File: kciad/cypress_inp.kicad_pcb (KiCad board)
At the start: 2 copper layers, 146.3 x 61.2 mm, 57 parts, among them J1 Cypress CY7C68013A Left Bot, J10 Conn_01x03_Male, J11 Conn_01x03_Male, J2 Connector PDx, J3 Cypress CY7C68013A Right Bot, J4 Connector PBx, J5 Power, J6 USB_B, J7 Conn_01x04_Male, J8 Conn_01x03_Male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

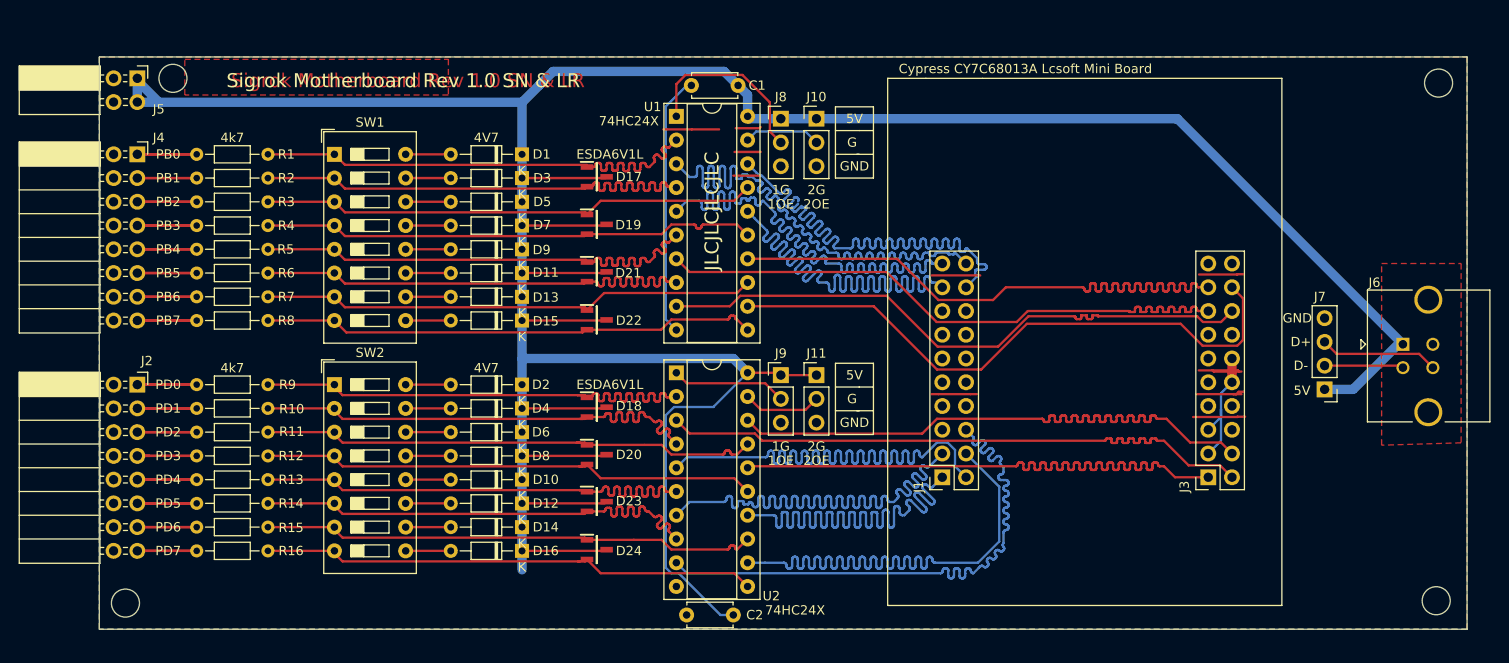
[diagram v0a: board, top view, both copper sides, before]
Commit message: * changed layout so signal paths are shorter
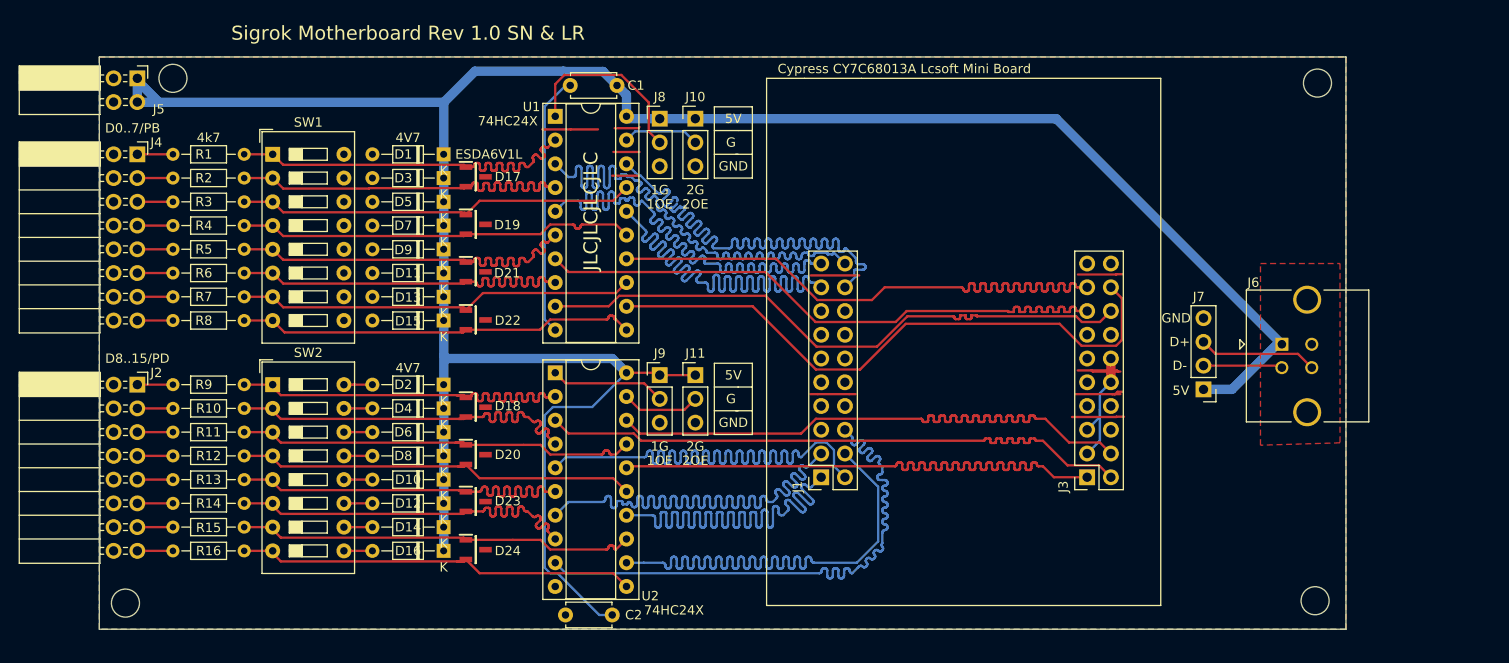
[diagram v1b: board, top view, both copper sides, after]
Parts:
- moved J1 13.0 mm to (136.4, 114.3)
- moved J3 13.0 mm to (164.8, 114.3)
- moved J7 13.0 mm to (177.3, 104.9)
- moved J8 13.0 mm to (119.1, 75.9)
- moved J9 13.0 mm to (119.1, 103.4)
- moved C1 13.0 mm to (114.6, 72.4)
- moved C2 13.0 mm to (114.0, 129.0)
- moved D17 13.0 mm to (99.4, 82.2)
- moved D18 13.0 mm to (99.4, 106.8)
- moved D19 13.0 mm to (99.4, 87.2)
- moved D20 13.0 mm to (99.4, 111.9)
- moved D21 13.0 mm to (99.4, 92.3)
- moved D22 13.0 mm to (99.4, 97.5)
- moved D23 13.0 mm to (99.4, 116.9)
- moved D24 13.0 mm to (99.4, 122.0)
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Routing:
- net +5V: track 360.7 -> 269.6 mm
- net B-PD0: track 15.7 -> 3.81 mm
- net /U1-1A0: track 53.1 -> 42.8 mm
- net /U1-2A0: track 53.9 -> 43.7 mm
- net /U2-2A2: track 53.2 -> 43.1 mm
- net /U2-2A1: track 53.2 -> 43.0 mm
- net /U1-1A2: track 53.0 -> 42.9 mm
- net /U1-1A1: track 53.3 -> 43.2 mm
- net /U1-1A3: track 53.3 -> 43.2 mm
- net /U1-2A2: track 53.0 -> 43.0 mm
- net /U1-2A1: track 53.6 -> 43.6 mm
- net /U2-1A0: track 53.6 -> 43.7 mm
- net /U1-2A3: track 53.3 -> 43.5 mm
- net B-PD3: track 13.5 -> 3.81 mm
- net B-PD1: track 13.5 -> 3.81 mm
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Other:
- board size 146.3 x 61.2 mm -> 133.4 x 61.2 mm
- board text added: "D0..7/PB"
- board text added: "D8..15/PD"
- board text removed: "PB0"
- board text removed: "PB1"
- board text removed: "PB2"
- board text removed: "PB3"
- board text removed: "PB4"
- board text removed: "PB5"
- board text removed: "PB6"
- board text removed: "PB7"
- board text removed: "PD0"
- board text removed: "PD1"
- board text removed: "PD2"
- board text removed: "PD3"
- board text removed: "PD4"
- board text removed: "PD5"
- board text removed: "PD6"
- board text removed: "PD7"

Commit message: * changed whole schematic and pcb layout
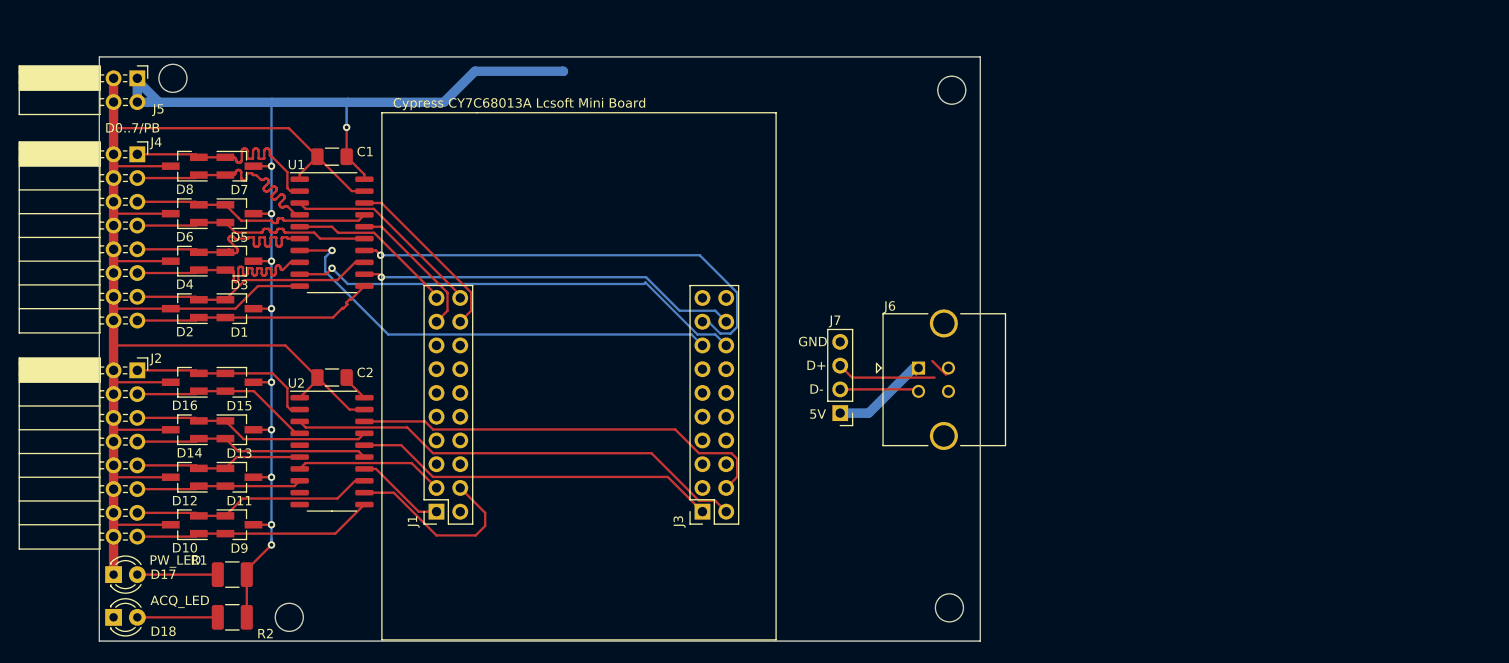
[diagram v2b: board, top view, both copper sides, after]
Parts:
- removed D19, D20, D21, D22, D23, D24: ESDA6V1L, SamacSys_Parts:SOT105P242X150-3N
- removed J10, J11, J8, J9: Conn_01x03_Male, Connector_PinHeader_2.54mm:PinHeader_1x03_P2.54mm_Vertical
- removed R10, R11, R12, R13, R14, R15, R16, R3, R4, R5, R6, R7, R8, R9: 4k7, Resistor_THT:R_Axial_DIN0204_L3.6mm_D1.6mm_P7.62mm_Horizontal
- removed SW1, SW2: SW_DIP_x08, Button_Switch_THT:SW_DIP_SPSTx08_Slide_9.78x22.5mm_W7.62mm_P2.54mm
- C1, C2: value C -> 100nF; footprint Capacitor_THT:C_Disc_D4.7mm_W2.5mm_P5.00mm -> Capacitor_SMD:C_1206_3216Metric_Pad1.33x1.80mm_HandSolder
- D1, D11, D13, D15, D3, D5, D7, D9: value 4V7 -> D_Schottky_x2_KCom_AAK; footprint Diode_THT:D_DO-34_SOD68_P7.62mm_Horizontal -> Package_TO_SOT_SMD:SOT-23_Handsoldering
- D10, D12, D14, D16, D2, D4, D6, D8: value 4V7 -> D_Schottky_x2_ACom_KKA; footprint Diode_THT:D_DO-34_SOD68_P7.62mm_Horizontal -> Package_TO_SOT_SMD:SOT-23_Handsoldering
- D17: value ESDA6V1L -> Power LED; footprint SamacSys_Parts:SOT105P242X150-3N -> LED_THT:LED_D3.0mm
- D18: value ESDA6V1L -> Acquisition LED; footprint SamacSys_Parts:SOT105P242X150-3N -> LED_THT:LED_D3.0mm
- R1, R2: value 4k7 -> 1k; footprint Resistor_THT:R_Axial_DIN0204_L3.6mm_D1.6mm_P7.62mm_Horizontal -> Resistor_SMD:R_1210_3225Metric_Pad1.30x2.65mm_HandSolder
- U1, U2: footprint Package_DIP:DIP-20_W7.62mm_Socket -> Package_SO:SO-20_5.3x12.6mm_P1.27mm
- moved D17 57.5 mm to (60.7, 124.7)
- moved R2 47.0 mm to (73.4, 129.3)
- moved R1 45.0 mm to (73.4, 124.7)
- moved D18 44.8 mm to (60.7, 129.3)
- moved D8 41.6 mm to (68.3, 81.0)
- moved J3 41.3 mm to (123.7, 118.0)
- moved J1 41.3 mm to (95.2, 118.0)
- moved C2 39.3 mm to (84.1, 103.6)
- moved J6 38.9 mm to (146.8, 102.6)
- moved J7 38.9 mm to (138.4, 107.4)
- moved D9 36.7 mm to (74.2, 119.4), turned to 0 degrees
- moved D6 36.2 mm to (68.3, 86.1)
- moved D16 33.0 mm to (68.3, 104.1)
- moved D4 31.9 mm to (68.3, 91.2)
- moved C1 31.4 mm to (84.1, 80.0)
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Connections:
- D1 pad 1: +5V -> B-PB6
- D1 pad 2: Net-(D1-Pad2) -> B-PB7
- D10 pad 1: +5V -> B-PD7
- D10 pad 2: Net-(D10-Pad2) -> B-PD6
- D11 pad 1: +5V -> B-PD4
- D11 pad 2: Net-(D11-Pad2) -> B-PD5
- D12 pad 1: +5V -> B-PD5
- D12 pad 2: Net-(D12-Pad2) -> B-PD4
- D13 pad 1: +5V -> B-PD2
- D13 pad 2: Net-(D13-Pad2) -> B-PD3
- D14 pad 1: +5V -> B-PD3
- D14 pad 2: Net-(D14-Pad2) -> B-PD2
- D15 pad 1: +5V -> B-PD0
- D15 pad 2: Net-(D15-Pad2) -> B-PD1
- D16 pad 1: +5V -> B-PD1
- D16 pad 2: Net-(D16-Pad2) -> B-PD0
- D17 pad 1: /U1-1A0 -> GND
- D17 pad 2: /U1-1A1 -> Net-(D17-Pad2)
- D18 pad 1: /U2-1A0 -> PA1
- D18 pad 2: /U2-1A1 -> Net-(D18-Pad2)
- D2 pad 1: +5V -> B-PB7
- D2 pad 2: Net-(D2-Pad2) -> B-PB6
- D3 pad 1: +5V -> B-PB4
- D3 pad 2: Net-(D3-Pad2) -> B-PB5
- D4 pad 1: +5V -> B-PB5
- D4 pad 2: Net-(D4-Pad2) -> B-PB4
- D5 pad 1: +5V -> B-PB2
- D5 pad 2: Net-(D5-Pad2) -> B-PB3
- D6 pad 1: +5V -> B-PB3
- D6 pad 2: Net-(D6-Pad2) -> B-PB2
- D7 pad 1: +5V -> B-PB0
- D7 pad 2: Net-(D7-Pad2) -> B-PB1
- D8 pad 1: +5V -> B-PB1
- D8 pad 2: Net-(D8-Pad2) -> B-PB0
- D9 pad 1: +5V -> B-PD6
- D9 pad 2: Net-(D9-Pad2) -> B-PD7
- J1 pad 11: Net-(J1-Pad11) -> PA1
- R1 pad 1: /U1-1A0 -> +5V
- R1 pad 2: B-PB0 -> Net-(D17-Pad2)
- R2 pad 1: /U1-1A1 -> +5V
- R2 pad 2: B-PB1 -> Net-(D18-Pad2)
- U1 pad 1: /U1-1OE -> GND
- U1 pad 11: /U1-2A3 -> B-PB7
- U1 pad 13: /U1-2A2 -> B-PB6
- U1 pad 15: /U1-1A3 -> B-PB3
- U1 pad 17: /U1-1A2 -> B-PB2
- U1 pad 19: /U1-2OE -> GND
- U1 pad 2: /U1-1A0 -> B-PB0
- U1 pad 4: /U1-1A1 -> B-PB1
- U1 pad 6: /U1-2A0 -> B-PB4
- U1 pad 8: /U1-2A1 -> B-PB5
- U2 pad 1: /U2-1OE -> GND
- U2 pad 11: /U2-2A3 -> B-PD7
- U2 pad 13: /U2-2A2 -> B-PD6
- U2 pad 15: /U2-1A3 -> B-PD3
- U2 pad 17: /U2-1A2 -> B-PD2
- U2 pad 19: /U2-2OE -> GND
- U2 pad 2: /U2-1A0 -> B-PD0
- U2 pad 4: /U2-1A1 -> B-PD1
- U2 pad 6: /U2-2A0 -> B-PD4
- U2 pad 8: /U2-2A1 -> B-PD5
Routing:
- net GND: track 91.4 -> 236.7 mm
- net +5V: track 269.6 -> 147.5 mm, vias 0 -> 10
- net PD0: track 65.3 -> 0.00 mm
- net PD4: track 65.2 -> 0.00 mm
- net PD3: track 65.2 -> 9.61 mm
- net PB6: track 65.2 -> 15.4 mm
- net PD1: track 65.2 -> 16.0 mm
- net PB4: track 65.2 -> 18.0 mm
- net PB7: track 65.3 -> 19.0 mm
- net PD2: track 65.2 -> 20.4 mm
- net /U2-1A2: track 44.3 -> 0.00 mm
- net /U2-2A0: track 44.2 -> 0.00 mm
- net /U2-1A3: track 43.9 -> 0.00 mm
- net /U2-2A3: track 43.8 -> 0.00 mm
- net /U2-1A1: track 43.8 -> 0.00 mm
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- removed copper zone on B.Cu, net GND
- removed copper zone on F.Cu, net GND
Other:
- board size 133.4 x 61.2 mm -> 94.2 x 62.5 mm
- board text added: "ACQ_LED"
- board text added: "PW_LED"
- board text removed: "1G"
- board text removed: "1OE"
- board text removed: "2G"
- board text removed: "2OE"
- board text removed: "4V7"
- board text removed: "4k7"
- board text removed: "74HC24X"
- board text removed: "D8..15/PD"
- board text removed: "ESDA6V1L"
- board text removed: "G"
- board text removed: "JLCJLCJLCJLC"
- board text removed: "Sigrok Motherboard Rev 1.0 SN & LR"

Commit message: * added gerber files, * copleted routing of pcb
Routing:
- net +5V: track 147.5 -> 206.5 mm, vias 10 -> 11
- net PA1: track 0.00 -> 51.9 mm
- net PD3: track 9.61 -> 49.9 mm
- net PB6: track 15.4 -> 48.4 mm
- net PB4: track 18.0 -> 50.2 mm
- net PD1: track 16.0 -> 47.3 mm
- net PB7: track 19.0 -> 50.0 mm
- net PD2: track 20.4 -> 50.0 mm
- net PB5: track 21.6 -> 48.6 mm
- net PD4: track 0.00 -> 24.2 mm, vias 0 -> 1
- net PD0: track 0.00 -> 18.4 mm, vias 0 -> 1
- net PB2: track 40.9 -> 52.0 mm
- net PD6: track 39.1 -> 49.9 mm
- net PD7: track 45.1 -> 49.9 mm
- net GND: track 236.7 -> 238.4 mm, vias 0 -> 1
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- added copper zone on B.Cu, net GND
- added copper zone on F.Cu, net GND
